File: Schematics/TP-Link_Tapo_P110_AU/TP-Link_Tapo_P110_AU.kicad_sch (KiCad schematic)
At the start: 9 parts

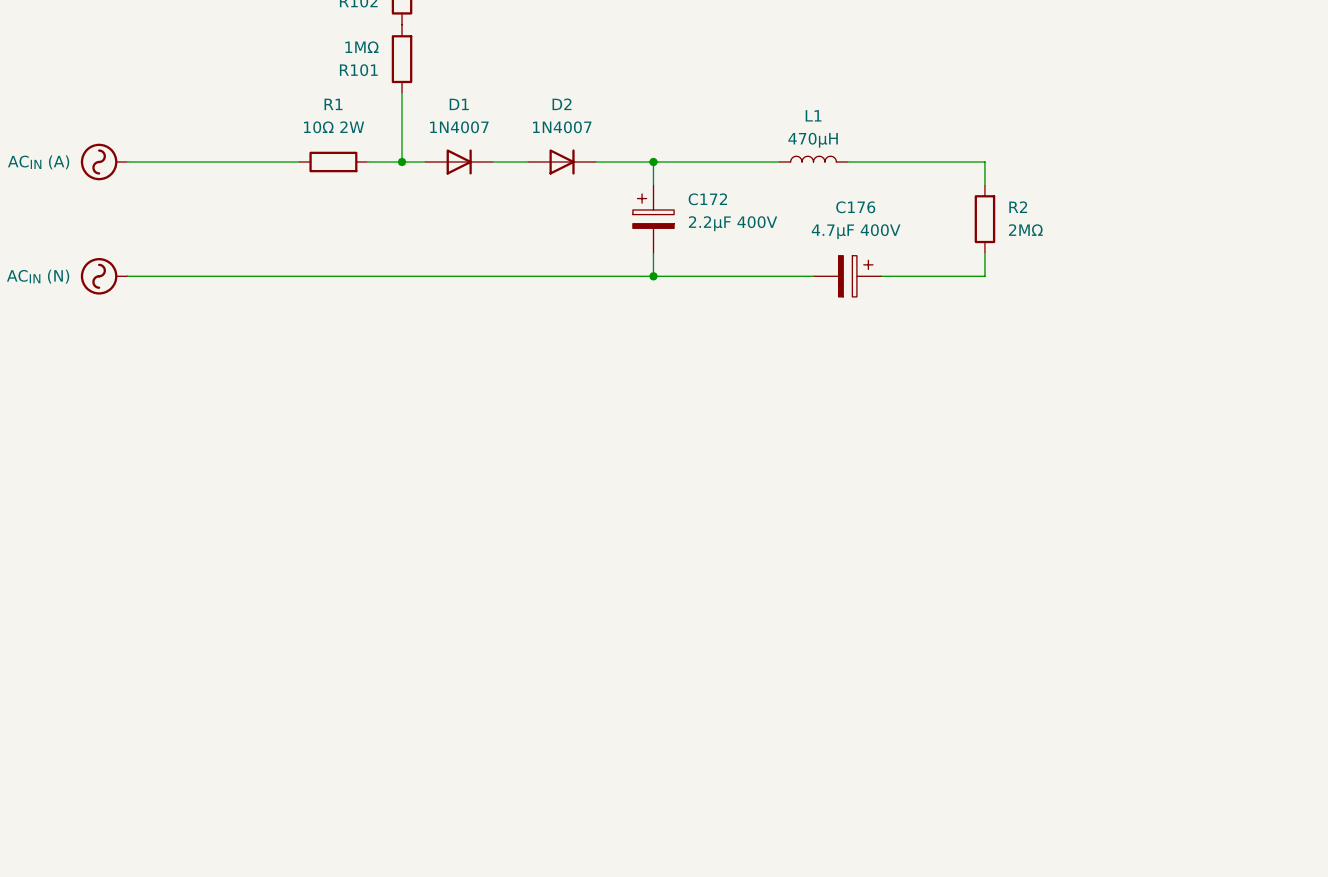
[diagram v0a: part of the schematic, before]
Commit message: Added Silergy SY22841
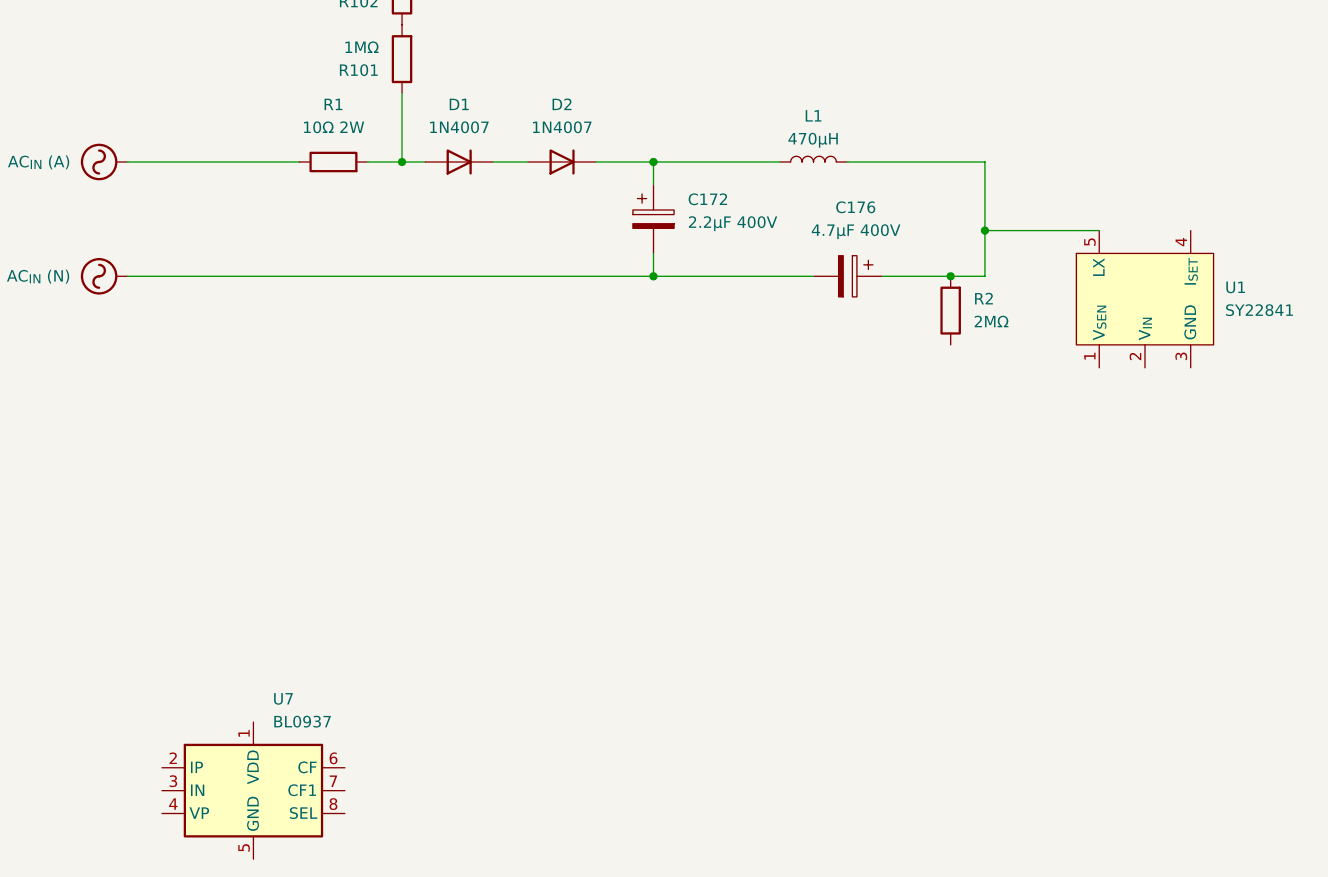
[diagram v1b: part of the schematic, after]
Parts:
- added U1: SY22841, Package_TO_SOT_SMD:SOT-23-5_HandSoldering, symbol TP-Link_Tapo_P110:SY22841
- added U7: BL0937, Package_SO:JEITA_SOIC-8_3.9x4.9mm_P1.27mm, symbol Sensor:BL0937
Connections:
- net at L1.2, R2.2: now also C176.1, U1.5 (LX)
- net at R2.1: no longer C176.1
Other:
- moved on the sheet: R2
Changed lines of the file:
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@@
+	)
+	(junction
+		(at 133.35 50.8)
+		(diameter 0)
+		(color 0 0 0 0)
 	)
 	(junction
@@
 	)
 	(junction
+		(at 129.54 55.88)
+		(diameter 0)
+		(color 0 0 0 0)
+	)
+	(junction
 		(at 96.52 43.18)
 		(diameter 0)
@@
 	(wire
 		(pts
+			(xy 129.54 55.88) (xy 133.35 55.88)
+		)
+		(stroke
+			(width 0)
+			(type default)
+		)
+	)
+	(wire
+		(pts
 			(xy 68.58 43.18) (xy 64.77 43.18)
 		)
@@
 	(wire
 		(pts
-			(xy 133.35 45.72) (xy 133.35 43.18)
+			(xy 133.35 50.8) (xy 146.05 50.8)
+		)
+		(stroke
+			(width 0)
+			(type default)
+		)
+	)
+	(wire
+		(pts
+			(xy 133.35 50.8) (xy 133.35 55.88)
 		)
 		(stroke
@@
 	(wire
 		(pts
-			(xy 121.92 55.88) (xy 133.35 55.88)
+			(xy 121.92 55.88) (xy 129.54 55.88)
 		)
 		(stroke
@@
 	(wire
 		(pts
-			(xy 133.35 55.88) (xy 133.35 53.34)
+			(xy 133.35 43.18) (xy 133.35 50.8)
 		)
 		(stroke
@@
 	)
 	(symbol
+		(lib_id "TP-Link_Tapo_P110:SY22841")
+		(at 151.13 50.8 0)
+		(unit 1)
+		(exclude_from_sim no)
+		(in_bom yes)
+		(on_board yes)
+		(dnp no)
+		(fields_autoplaced yes)
+		(property "Reference" "U1"
+			(at 160.02 57.1499 0)
+			(effects
+				(font
+					(size 1.27 1.27)
+				)
+				(justify left)
+			)
+		)
+		(property "Value" "SY22841"
+			(at 160.02 59.6899 0)
+			(effects
+				(font
+					(size 1.27 1.27)
+				)
+				(justify left)
+			)
+		)
+		(property "Footprint" "Package_TO_SOT_SMD:SOT-23-5_HandSoldering"
+			(at 151.13 50.8 0)
+			(effects
+				(font
+					(size 1.27 1.27)
+				)
+				(hide yes)
+			)
+		)
+		(property "Datasheet" ""
+			(at 151.13 50.8 0)
+			(effects
+				(font
+					(size 1.27 1.27)
+				)
+				(hide yes)
+			)
+		)
+		(property "Description" ""
+			(at 151.13 50.8 0)
+			(effects
+				(font
+					(size 1.27 1.27)
+				)
+				(hide yes)
+			)
+		)
+		(pin "4"
+		)
+		(pin "1"
+		)
+		(pin "2"
+		)
+		(pin "5"
+		)
+		(pin "3"
+		)
+		(instances
+			(project ""
+				(path "/7315a680-fa54-4737-88bc-efa2941399e6"
+					(reference "U1")
+					(unit 1)
+				)
+			)
+		)
+	)
+	(symbol
 		(lib_id "Device:L")
 		(at 114.3 43.18 90)
@@
 	(symbol
 		(lib_id "Device:R")
-		(at 133.35 49.53 180)
+		(at 129.54 59.69 180)
 		(unit 1)
 		(exclude_from_sim no)
@@
 		(fields_autoplaced yes)
 		(property "Reference" "R2"
-			(at 135.89 48.2599 0)
+			(at 132.08 58.4199 0)
 			(effects
 				(font
@@
 		)
 		(property "Value" "2MΩ"
-			(at 135.89 50.7999 0)
+			(at 132.08 60.9599 0)
 			(effects
 				(font
@@
 		)
 		(property "Footprint" "Resistor_SMD:R_1206_3216Metric"
-			(at 135.128 49.53 90)
+			(at 131.318 59.69 90)
 			(effects
 				(font
@@
 		)
 		(property "Datasheet" "~"
-			(at 133.35 49.53 0)
+			(at 129.54 59.69 0)
 			(effects
 				(font
@@
 		)
 		(property "Description" "Resistor"
-			(at 133.35 49.53 0)
+			(at 129.54 59.69 0)
 			(effects
 				(font
@@
 		)
 		(instances
-			(project ""
+			(project "TP-Link_Tapo_P110_AU"
 				(path "/7315a680-fa54-4737-88bc-efa2941399e6"
 					(reference "R2")
@@
 					(unit 1)
 				)
+			)
+		)
+	)
+	(symbol
+		(lib_id "Sensor:BL0937")
+		(at 52.07 113.03 0)
+		(unit 1)
+		(exclude_from_sim no)
+		(in_bom yes)
+		(on_board yes)
+		(dnp no)
+		(fields_autoplaced yes)
+		(property "Reference" "U7"
+			(at 54.2133 102.87 0)
+			(effects
+				(font
+					(size 1.27 1.27)
+				)
+				(justify left)
+			)
+		)
+		(property "Value" "BL0937"
+			(at 54.2133 105.41 0)
+			(effects
+				(font
+					(size 1.27 1.27)
+				)
+				(justify left)
+			)
+		)
+		(property "Footprint" "Package_SO:JEITA_SOIC-8_3.9x4.9mm_P1.27mm"
+			(at 54.61 130.81 0)
+			(effects
+				(font
+					(size 1.27 1.27)
+				)
+				(hide yes)
+			)
+		)
+		(property "Datasheet" "https://www.belling.com.cn/media/file_object/bel_product/BL0937/datasheet/BL0937_V1.02_en.pdf"
+			(at 52.07 113.03 0)
+			(effects
+				(font
+					(size 1.27 1.27)
+				)
+				(hide yes)
+			)
+		)
+		(property "Description" "Single Phase Energy Meter IC with Integrated Oscillator, JEITA SOIC-8 (SOP-8)"
+			(at 52.07 113.03 0)
+			(effects
+				(font
+					(size 1.27 1.27)
+				)
+				(hide yes)
+			)
+		)
+		(pin "6"
+		)
+		(pin "3"
+		)
+		(pin "4"
+		)
+		(pin "1"
+		)
+		(pin "5"
+		)
+		(pin "2"
+		)
+		(pin "8"
+		)
+		(pin "7"
+		)
+		(instances
+			(project ""
+				(path "/7315a680-fa54-4737-88bc-efa2941399e6"
+					(reference "U7")
+					(unit 1)
+				)

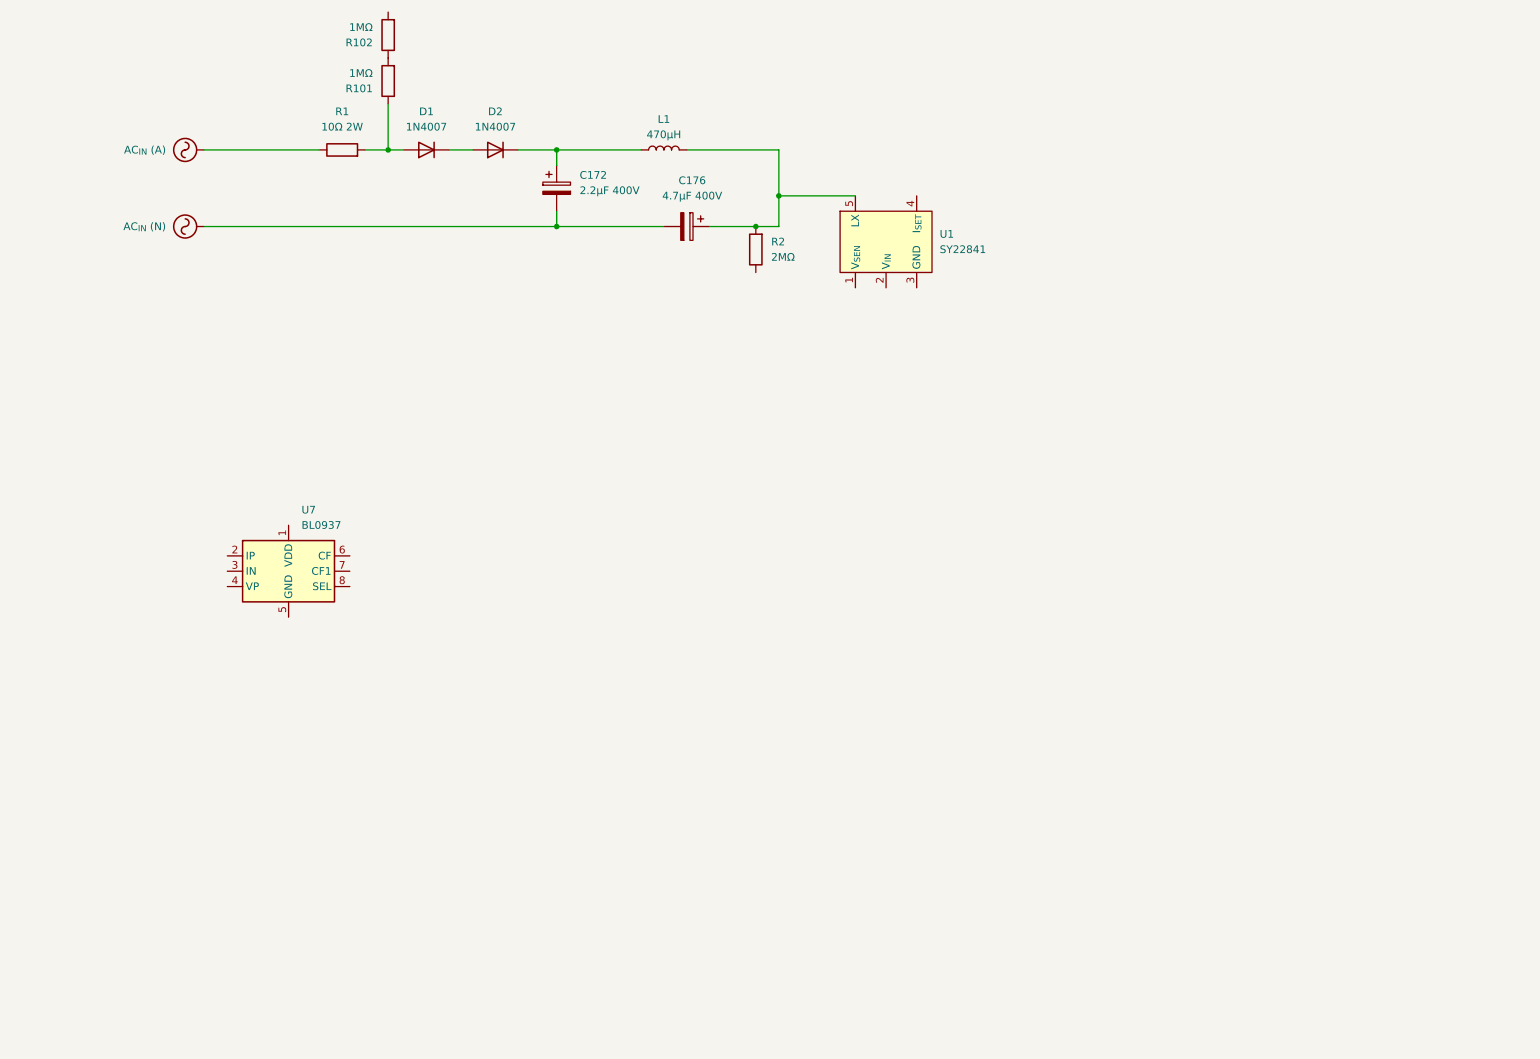
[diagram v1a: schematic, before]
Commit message: Update TP-Link_Tapo_P110_AU.kicad_sch
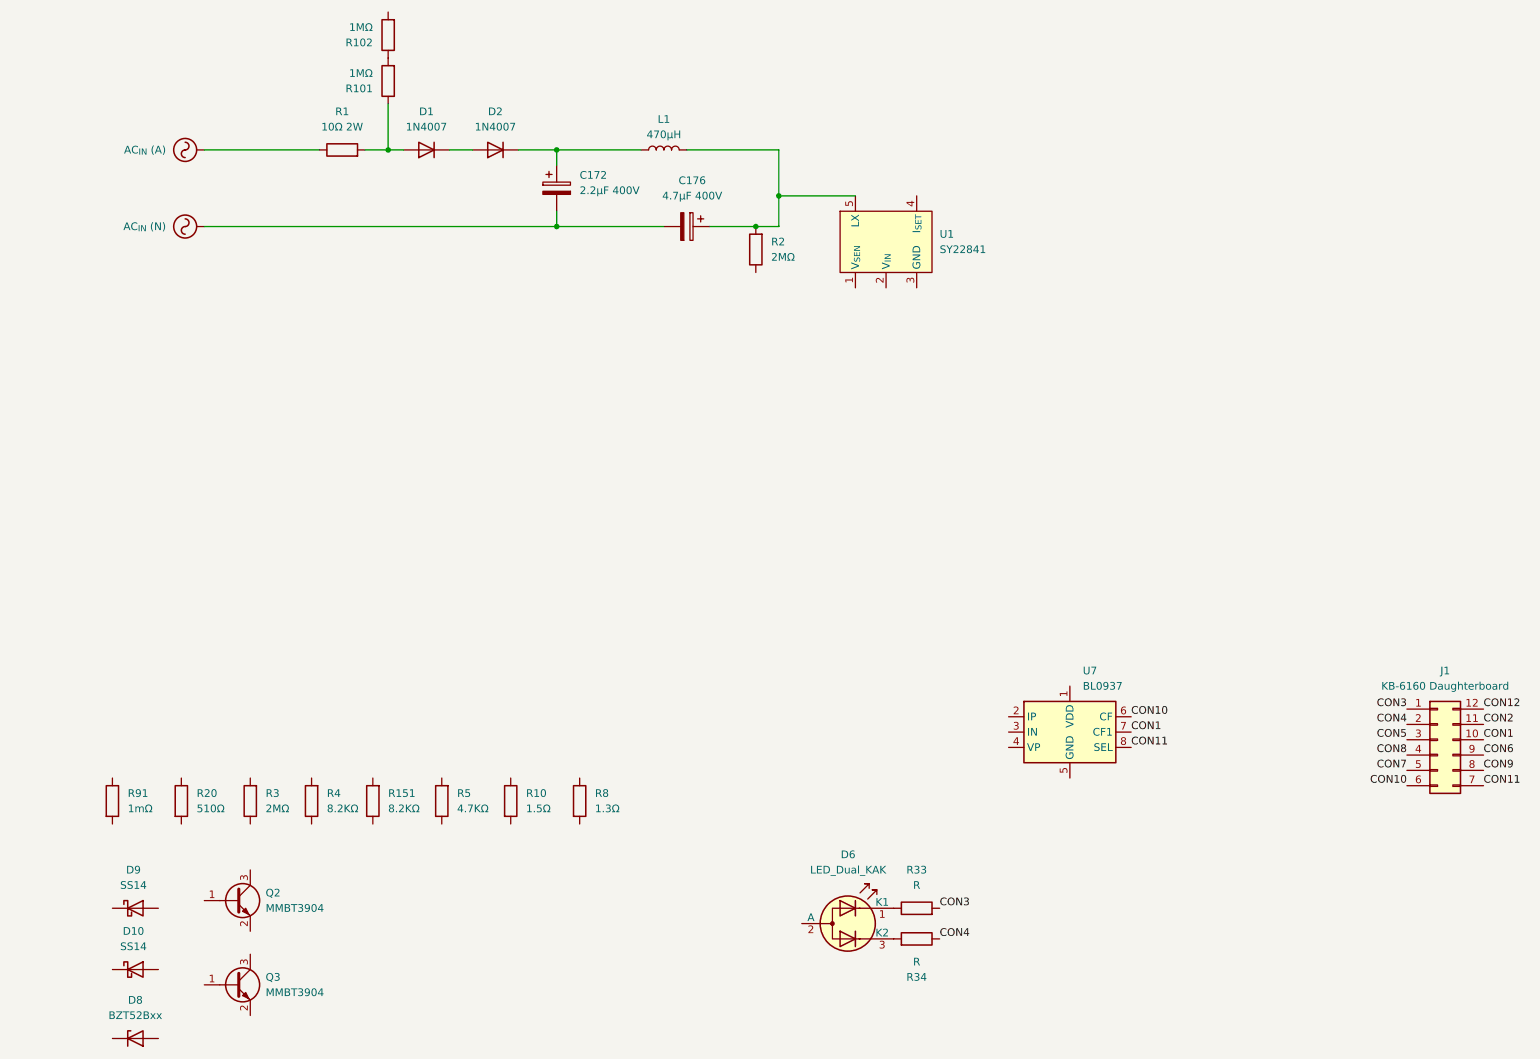
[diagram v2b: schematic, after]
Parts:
- added D10, D9: SS14, Diode_SMD:D_SMA, symbol Diode:SS14
- added D6: LED_Dual_KAK, symbol Device:LED_Dual_KAK
- added D8: BZT52Bxx, Diode_SMD:D_SOD-123F, symbol Diode:BZT52Bxx
- added J1: KB-6160 Daughterboard, symbol Connector_Generic:Conn_02x06_Counter_Clockwise
- added Q2, Q3: MMBT3904, Package_TO_SOT_SMD:SOT-23, symbol Transistor_BJT:MMBT3904
- added R10: 1.5Ω, Resistor_SMD:R_1206_3216Metric, symbol Device:R
- added R151, R4: 8.2KΩ, Resistor_SMD:R_1206_3216Metric, symbol Device:R
- added R20: 510Ω, Resistor_SMD:R_0603_1608Metric_Pad0.98x0.95mm_HandSolder, symbol Device:R
- added R3: 2MΩ, Resistor_SMD:R_1206_3216Metric, symbol Device:R
- added R33, R34: R, symbol Device:R
- added R5: 4.7KΩ, Resistor_SMD:R_0603_1608Metric_Pad0.98x0.95mm_HandSolder, symbol Device:R
- added R8: 1.3Ω, Resistor_SMD:R_0805_2012Metric_Pad1.20x1.40mm_HandSolder, symbol Device:R
- added R91: 1mΩ, Resistor_SMD:R_2512_6332Metric_Pad1.40x3.35mm_HandSolder, symbol Device:R
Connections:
- net CON10: now reaches U7.6 (CF)
- net CON10: now also J1.6 (Pin_6)
- net CON1: now reaches U7.7 (CF1)
- net CON1: now also J1.10 (Pin_10)
- net CON11: now reaches U7.8 (SEL)
- net CON11: now also J1.7 (Pin_7)
- new net: D6.3 (K2), R34.2
- new net: D6.1 (K1), R33.1
- new net CON12: J1.12 (Pin_12)
- new net CON2: J1.11 (Pin_11)
- new net CON3: J1.1 (Pin_1), R33.2
- new net CON4: J1.2 (Pin_2), R34.1
- new net CON5: J1.3 (Pin_3)
- new net CON6: J1.9 (Pin_9)
- new net CON7: J1.5 (Pin_5)
- new net CON8: J1.4 (Pin_4)
- new net CON9: J1.8 (Pin_8)
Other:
- moved on the sheet: U7
